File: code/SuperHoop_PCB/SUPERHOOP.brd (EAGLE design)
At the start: 100 x 16.5 mm, 11 parts, among them CON1 Battery_lithium 3.7v (3x), CON2 TOUCH_INPUT, CON3 LED_STRING_OUTPUT, CON4 ADXL335_BBOARD_V2, CON5 ISP-AVR_6P, IC1 MEGA8-P

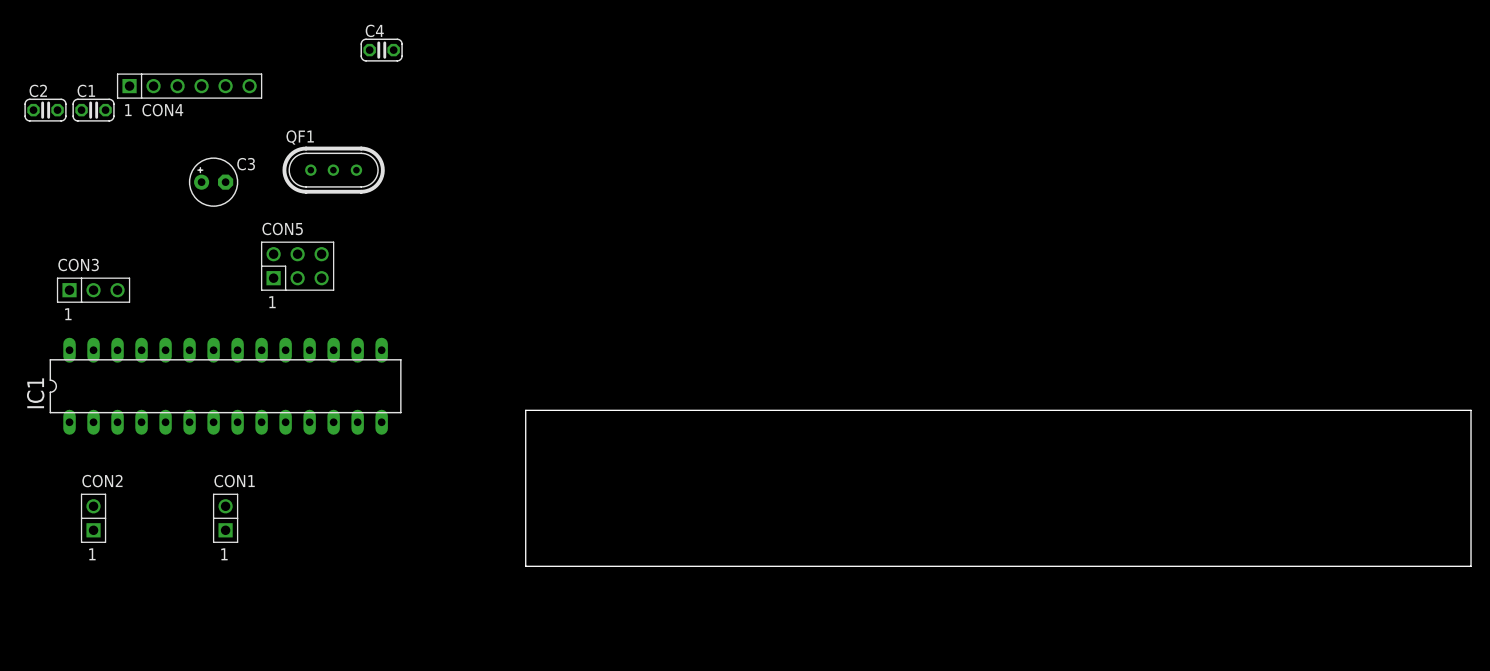
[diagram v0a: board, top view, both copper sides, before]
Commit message: final changes from Sunday
Saved Eagle files, shortened delay between pattern cycles to ~5 seconds
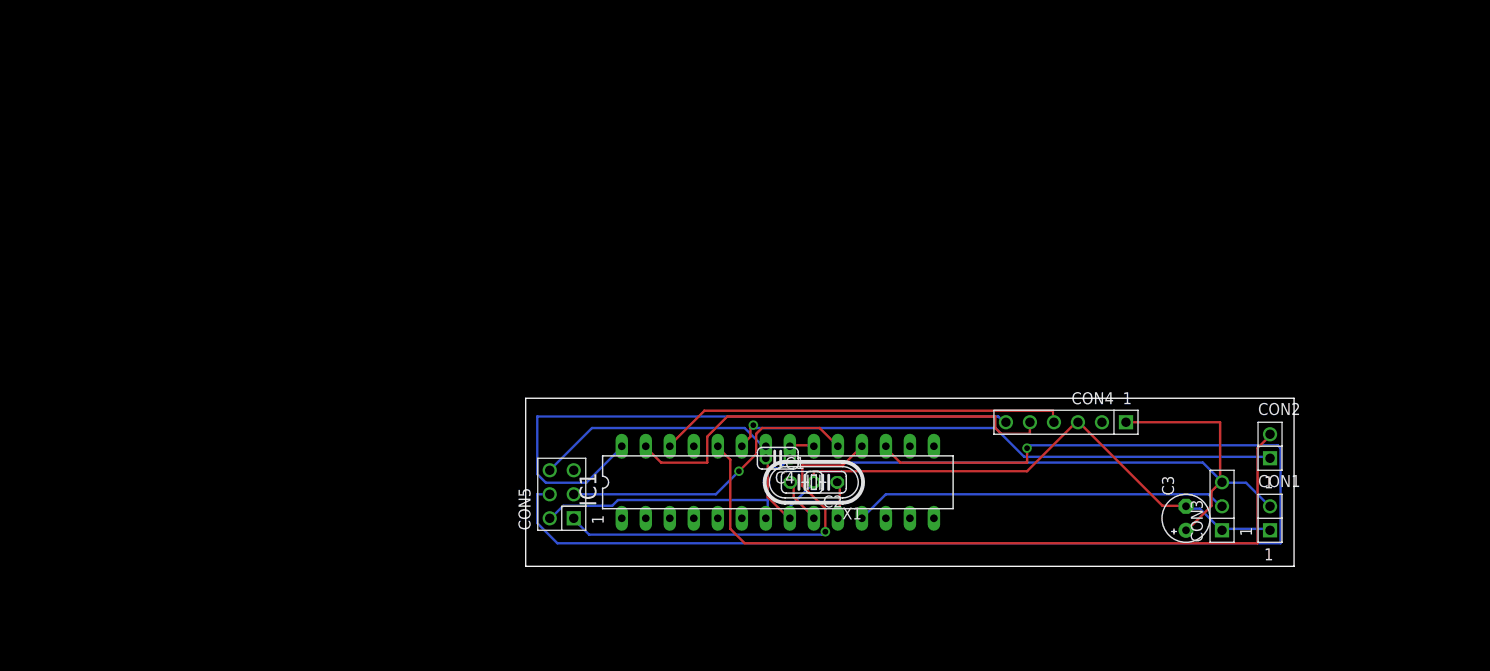
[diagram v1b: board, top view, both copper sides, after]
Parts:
- removed QF1: 8M10AHC49T, crystal:HC49U
- added X1: (no value), crystal:HC49/S
- moved CON2 124.7 mm to (78.7, 12.7)
- moved CON3 121.5 mm to (73.7, 6.35), turned to 90 degrees
- moved CON1 110.5 mm to (78.7, 5.08)
- moved C3 108.8 mm to (69.8, 5.08), turned to 90 degrees
- moved CON4 99.3 mm to (57.1, 15.2), turned to 180 degrees
- moved C2 91.5 mm to (31.8, 8.89), turned to 180 degrees
- moved C1 84.6 mm to (29.2, 8.89)
- moved C4 60.2 mm to (26.7, 11.4), turned to 180 degrees
- moved IC1 59.3 mm to (26.7, 8.89)
- moved CON5 36.9 mm to (3.81, 7.62), turned to 90 degrees
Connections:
- net GND: no longer QF1.2
- net MISO: now also IC1.18
- net MOSI: now also IC1.17
- net SCK: now also IC1.19
- net XTAL1: now also X1.2; no longer QF1.1
- net XTAL2: now also X1.1; no longer QF1.3
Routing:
- net MOSI: track 0.00 -> 138.3 mm, vias 0 -> 1
- net VCC: track 0.00 -> 112.4 mm
- net GND: track 0.00 -> 95.8 mm
- net TOUCHB: track 0.00 -> 77.7 mm
- net XOUT: track 0.00 -> 66.9 mm
- net TOUCHA: track 0.00 -> 58.9 mm, vias 0 -> 1
- net YOUT: track 0.00 -> 47.7 mm
- net ZOUT: track 0.00 -> 43.5 mm
- net MISO: track 0.00 -> 42.7 mm, vias 0 -> 1
- net DOUT: track 0.00 -> 39.7 mm
- net SCK: track 0.00 -> 32.9 mm, vias 0 -> 1
- net XTAL1: track 0.00 -> 5.22 mm
- net XTAL2: track 0.00 -> 4.43 mm
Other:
- board size 100 x 16.5 mm -> 81.3 x 17.8 mm

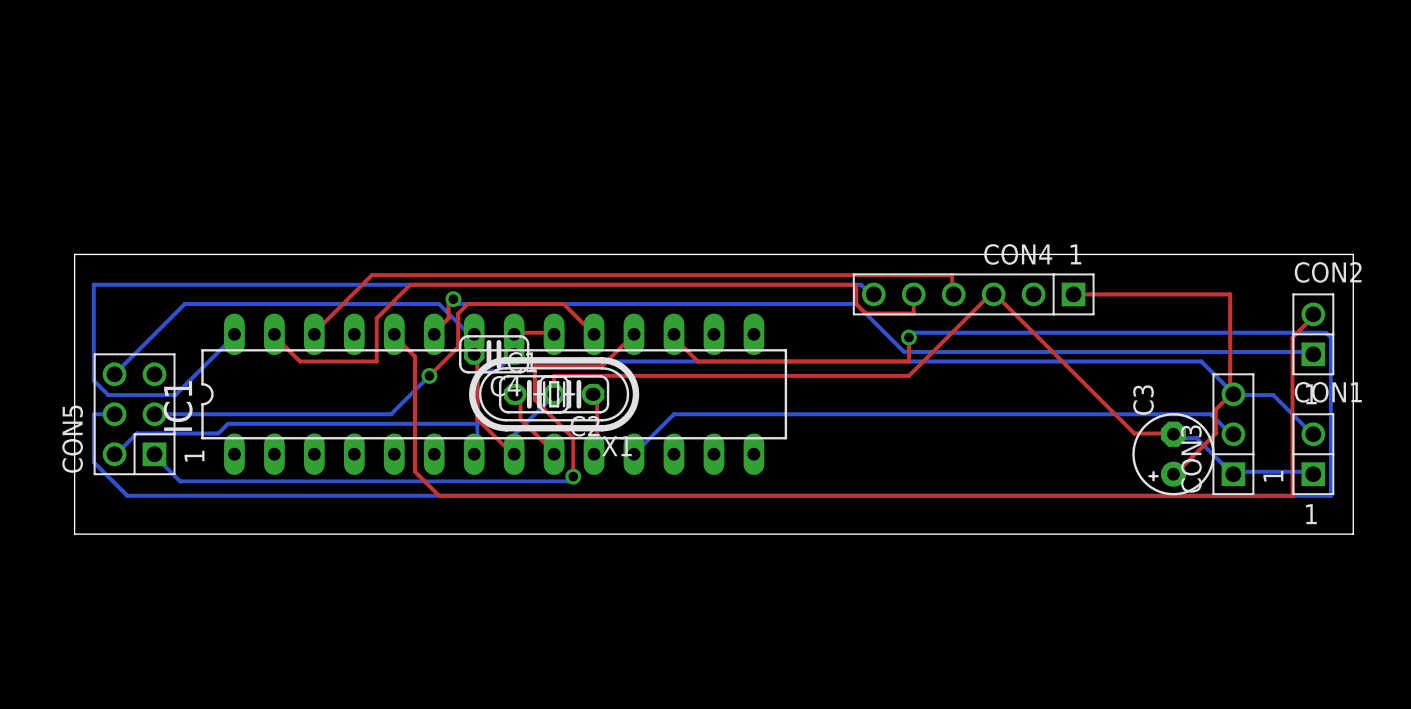
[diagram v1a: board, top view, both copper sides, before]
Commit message: Fixed wrong wiring
made the board wiring more readable
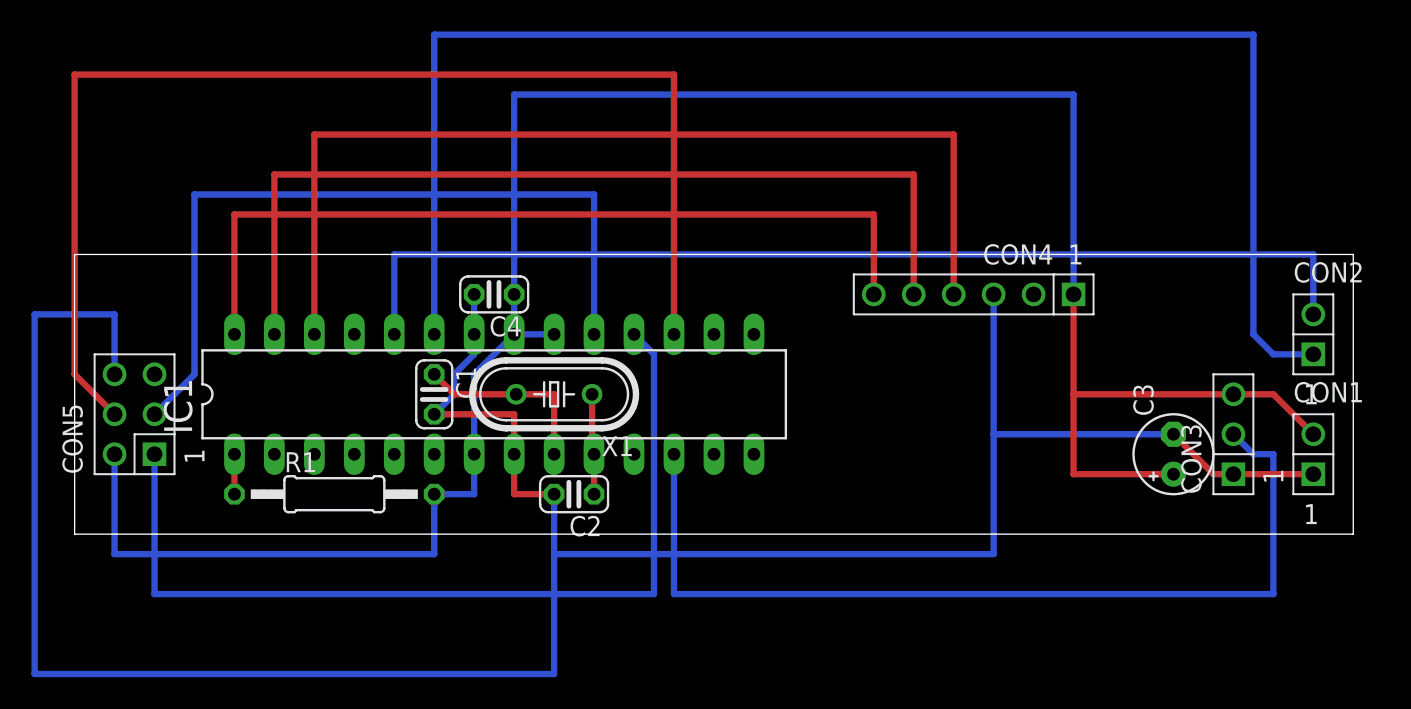
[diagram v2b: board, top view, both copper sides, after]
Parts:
- added R1: 10k, rcl:0207/12
- moved C1 6.35 mm to (22.9, 8.89), turned to 270 degrees
- moved C2 6.35 mm to (31.8, 2.54)
- moved C4 3.81 mm to (26.7, 15.2)
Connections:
- new net N$1: IC1.1, R1.1
- net DOUT: now also IC1.12; no longer IC1.11
- net VCC: now also R1.2
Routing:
- net GND: track 95.8 -> 163.4 mm
- net MOSI: track 138.3 -> 77.3 mm, vias 1 -> 0
- net TOUCHA: track 58.9 -> 94.5 mm, vias 1 -> 0
- net VCC: track 112.4 -> 144.3 mm
- net ZOUT: track 43.5 -> 63.5 mm
- net DOUT: track 39.7 -> 58.9 mm
- net SCK: track 32.9 -> 49.3 mm, vias 1 -> 0
- net MISO: track 42.7 -> 57.7 mm, vias 1 -> 0
- net XOUT: track 66.9 -> 53.3 mm
- net YOUT: track 47.7 -> 58.4 mm
- net TOUCHB: track 77.7 -> 67.3 mm
- net XTAL1: track 5.22 -> 12.0 mm
- net N$1: track 0.00 -> 2.54 mm
- net XTAL2: track 4.43 -> 6.48 mm

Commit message: Converted patterns to const
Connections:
- removed net N$1: IC1.1, R1.1
- net RST: now also IC1.1, R1.1
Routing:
- net RST: track 0.00 -> 10.5 mm
- net N$1: track 2.54 -> 0.00 mm
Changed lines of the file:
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@@
 <layer number="20" name="Dimension" color="15" fill="1" visible="yes" active="yes"/>
 <layer number="21" name="tPlace" color="7" fill="1" visible="yes" active="yes"/>
-<layer number="22" name="bPlace" color="7" fill="1" visible="yes" active="yes"/>
+<layer number="22" name="bPlace" color="7" fill="1" visible="no" active="yes"/>
 <layer number="23" name="tOrigins" color="15" fill="1" visible="yes" active="yes"/>
 <layer number="24" name="bOrigins" color="15" fill="1" visible="yes" active="yes"/>
@@
 <layer number="37" name="tTest" color="7" fill="1" visible="no" active="yes"/>
 <layer number="38" name="bTest" color="7" fill="1" visible="no" active="yes"/>
-<layer number="39" name="tKeepout" color="4" fill="11" visible="yes" active="yes"/>
-<layer number="40" name="bKeepout" color="1" fill="11" visible="yes" active="yes"/>
-<layer number="41" name="tRestrict" color="4" fill="10" visible="yes" active="yes"/>
-<layer number="42" name="bRestrict" color="1" fill="10" visible="yes" active="yes"/>
-<layer number="43" name="vRestrict" color="2" fill="10" visible="yes" active="yes"/>
+<layer number="39" name="tKeepout" color="4" fill="11" visible="no" active="yes"/>
+<layer number="40" name="bKeepout" color="1" fill="11" visible="no" active="yes"/>
+<layer number="41" name="tRestrict" color="4" fill="10" visible="no" active="yes"/>
+<layer number="42" name="bRestrict" color="1" fill="10" visible="no" active="yes"/>
+<layer number="43" name="vRestrict" color="2" fill="10" visible="no" active="yes"/>
 <layer number="44" name="Drills" color="7" fill="1" visible="no" active="yes"/>
 <layer number="45" name="Holes" color="7" fill="1" visible="no" active="yes"/>
@@
 <signal name="RST">
 <contactref element="CON5" pad="5"/>
+<contactref element="R1" pad="1"/>
+<contactref element="IC1" pad="1"/>
+<wire x1="10.16" y1="2.54" x2="10.16" y2="5.08" width="0.4064" layer="1"/>
+<wire x1="5.08" y1="10.16" x2="6.35" y2="10.16" width="0.4064" layer="1"/>
+<wire x1="6.35" y1="10.16" x2="10.16" y2="6.35" width="0.4064" layer="1"/>
+<wire x1="10.16" y1="6.35" x2="10.16" y2="5.08" width="0.4064" layer="1"/>
 </signal>
 <signal name="MOSI">
@@
 <wire x1="38.1" y1="29.21" x2="38.1" y2="12.7" width="0.4064" layer="1"/>
 </signal>
-<signal name="N$1">
-<contactref element="R1" pad="1"/>
-<contactref element="IC1" pad="1"/>
-<wire x1="10.16" y1="2.54" x2="10.16" y2="5.08" width="0.4064" layer="1"/>
-</signal>
 </signals>
